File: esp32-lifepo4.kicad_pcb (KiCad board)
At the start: 2 copper layers, 15 parts, among them J1 Conn_01x12, J2 Conn_01x12, U1 ESP32-WROOM-32, U2 CN3058C, U3 TPS709

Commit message: v0
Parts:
- removed ?: , Aesthetics:OSHW-LOGO-L
- removed D1: DIODE, Diodes_SMD:D_SMA
- C2: value 4.7-10uF -> 10uF
- D2: value LED -> DONE
- D3: value LED -> CHRG
- R1: value 100 -> 100 ohms
- R2: value 2.463k -> 2.463k ohms
- R3: value 0 -> 0ohm
- U2: value CN3058C -> CN3058E
- moved JP1 0.92 mm to (166.4, 98.3)
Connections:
- C1 pad 2: Net-(C1-Pad2) -> VIN
- R1 pad 2: Net-(C1-Pad2) -> VIN
- U2 pad 4: Net-(C1-Pad2) -> VIN
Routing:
- net BAT+: track 54.9 -> 44.9 mm, vias 3 -> 1
- net Net-(C1-Pad2): track 9.95 -> 0.00 mm
- net 3V3: track 46.2 -> 42.2 mm

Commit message: minor changes
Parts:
- R2: value 2.463k ohms -> 2.463k
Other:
- board outline added: 28.4 x 31 mm
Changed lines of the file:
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@@
     (47 F.CrtYd user)
     (48 B.Fab user)
-    (49 F.Fab user)
+    (49 F.Fab user hide)
   )
   (setup
@@
     (trace_min 0.2)
     (segment_width 0.2)
-    (edge_width 0.15)
+    (edge_width 0.2)
     (via_size 0.8)
     (via_drill 0.4)
@@
     (tags "capacitor 0805")
     (attr smd)
-    (fp_text reference C1 (at -0.254 1.27 90) (layer F.SilkS)
+    (fp_text reference C1 (at -0.762 -1.524 90) (layer F.SilkS)
       (effects (font (size 1 1) (thickness 0.15)))
     )
@@
     (tags "capacitor 0805")
     (attr smd)
-    (fp_text reference C2 (at 0.762 1.778 270) (layer F.SilkS)
+    (fp_text reference C2 (at 0 1.524 270) (layer F.SilkS)
       (effects (font (size 1 1) (thickness 0.15)))
     )
@@
       (effects (font (size 0.6096 0.6096) (thickness 0.127)))
     )
-    (fp_text value "2.463k ohms" (at 0 1.27 90) (layer F.SilkS)
+    (fp_text value 2.463k (at 0 -1.27 90) (layer F.SilkS)
       (effects (font (size 0.6096 0.6096) (thickness 0.127)))
     )
@@
       (effects (font (size 0.6096 0.6096) (thickness 0.127)))
     )
-    (fp_text value 0ohm (at 0.254 -1.27 90) (layer F.SilkS)
+    (fp_text value 0ohm (at 1.016 -1.27 90) (layer F.SilkS)
       (effects (font (size 0.6096 0.6096) (thickness 0.127)))
     )
@@
     (effects (font (size 1.5 1.5) (thickness 0.3)) (justify mirror))
   )
-  (gr_line (start 143.256 100.584) (end 143.256 69.596) (layer Eco2.User) (width 0.2))
-  (gr_line (start 171.704 100.584) (end 143.256 100.584) (layer Eco2.User) (width 0.2))
-  (gr_line (start 171.704 69.596) (end 171.704 100.584) (layer Eco2.User) (width 0.2))
-  (gr_line (start 143.256 69.596) (end 171.704 69.596) (layer Eco2.User) (width 0.2))
+  (gr_line (start 143.256 100.584) (end 143.256 69.596) (layer Edge.Cuts) (width 0.2))
+  (gr_line (start 171.704 100.584) (end 143.256 100.584) (layer Edge.Cuts) (width 0.2))
+  (gr_line (start 171.704 69.596) (end 171.704 100.584) (layer Edge.Cuts) (width 0.2))
+  (gr_line (start 143.256 69.596) (end 171.704 69.596) (layer Edge.Cuts) (width 0.2))
   (via (at 153.162 96.9645) (size 0.8) (drill 0.4) (layers F.Cu B.Cu) (net 1))
   (segment (start 151.892 97.774) (end 152.3525 97.774) (width 0.25) (layer F.Cu) (net 1) (status 30))
@@
   (segment (start 157.093185 82.146599) (end 157.18 82.059784) (width 0.25) (layer F.Cu) (net 1))
   (segment (start 156.5275 82.146599) (end 157.093185 82.146599) (width 0.25) (layer F.Cu) (net 1))
-  (segment (start 154.78 96.2965) (end 154.78 96.139) (width 0.25) (layer F.Cu) (net 3) (status 30))
-  (segment (start 156.58084 98.09734) (end 154.78 96.2965) (width 0.25) (layer F.Cu) (net 3) (status 30))
-  (segment (start 156.58084 98.298) (end 156.58084 98.09734) (width 0.25) (layer F.Cu) (net 3) (status 30))
-  (segment (start 152.257 96.139) (end 151.892 95.774) (width 0.25) (layer F.Cu) (net 3) (status 30))
-  (segment (start 154.78 96.139) (end 152.257 96.139) (width 0.25) (layer F.Cu) (net 3) (status 30))
-  (segment (start 151.892 95.774) (end 151.767 95.774) (width 0.25) (layer F.Cu) (net 3) (status 30))
   (segment (start 162.703 96.139) (end 163.068 95.774) (width 0.4) (layer F.Cu) (net 2) (status 30))
   (segment (start 160.18 96.139) (end 162.703 96.139) (width 0.4) (layer F.Cu) (net 2) (status 30))
@@
   (segment (start 165.166 92.964) (end 165.1 93.03) (width 0.4) (layer F.Cu) (net 2))
   (segment (start 168.402 92.964) (end 165.166 92.964) (width 0.4) (layer F.Cu) (net 2))
+  (segment (start 154.78 96.2965) (end 154.78 96.139) (width 0.25) (layer F.Cu) (net 3) (status 30))
+  (segment (start 156.58084 98.09734) (end 154.78 96.2965) (width 0.25) (layer F.Cu) (net 3) (status 30))
+  (segment (start 156.58084 98.298) (end 156.58084 98.09734) (width 0.25) (layer F.Cu) (net 3) (status 30))
+  (segment (start 152.257 96.139) (end 151.892 95.774) (width 0.25) (layer F.Cu) (net 3) (status 30))
+  (segment (start 154.78 96.139) (end 152.257 96.139) (width 0.25) (layer F.Cu) (net 3) (status 30))
+  (segment (start 151.892 95.774) (end 151.767 95.774) (width 0.25) (layer F.Cu) (net 3) (status 30))
   (via (at 153.0985 75.8825) (size 0.8) (drill 0.4) (layers F.Cu B.Cu) (net 3))
   (segment (start 144.78 73.66) (end 150.876 73.66) (width 0.4) (layer B.Cu) (net 3) (status 10))

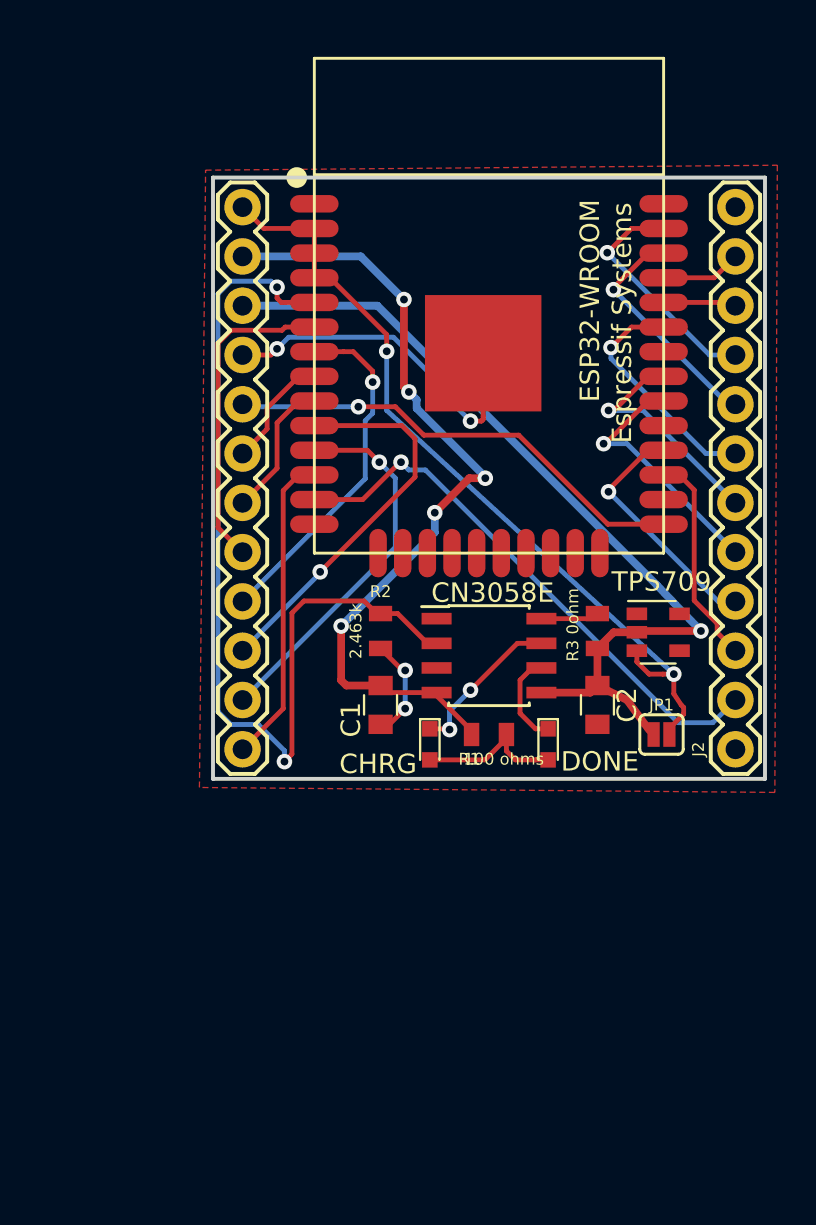
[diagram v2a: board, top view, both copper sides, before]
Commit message: Added symbol and footprint. Removed non-slim version
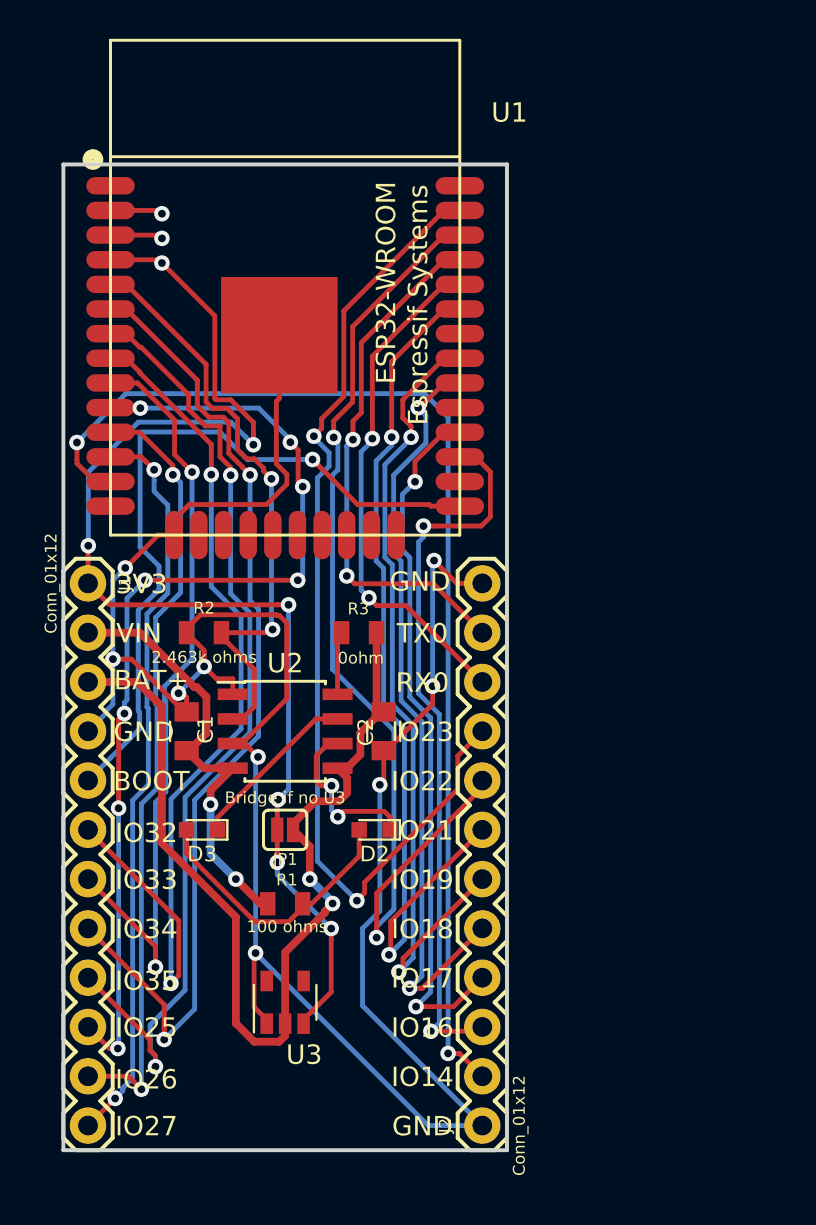
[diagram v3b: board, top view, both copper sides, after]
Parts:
- added REF***: OSHW-Symbol_13.4x12mm_SilkScreen, Symbols:OSHW-Symbol_13.4x12mm_SilkScreen, B.Cu at (147.4, 110.8)
- JP1: value SolderJumper_2_Open -> Bridge if no U3
- R2: value 2.463k -> 2.463k ohms
- moved U3 27.1 mm to (147.0, 112.1), turned to 90 degrees
- moved J2 23.4 mm to (157.1, 118.5)
- moved J1 21.0 mm to (136.8, 90.5)
- moved JP1 20.0 mm to (147.0, 103.2), turned to 180 degrees
- moved R1 13.7 mm to (147.0, 107.0)
- moved D3 12.5 mm to (142.7, 103.2), turned to 180 degrees
- moved R3 12.3 mm to (150.8, 93.1), turned to 180 degrees
- moved U2 11.2 mm to (147.0, 98.1)
- moved C2 11.1 mm to (152.1, 98.1)
- moved U1 10.5 mm to (147.0, 75.3)
- moved C1 10.1 mm to (141.9, 98.1), turned to 270 degrees
- moved D2 9.97 mm to (151.6, 103.2), turned to 180 degrees
- moved R2 9.10 mm to (142.8, 93.1), turned to 0 degrees
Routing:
- net GND: track 23.5 -> 121.5 mm, vias 4 -> 10
- net IO32: track 5.98 -> 47.8 mm, vias 0 -> 2
- net IO22: track 12.2 -> 52.2 mm, vias 1 -> 2
- net IO23: track 12.2 -> 52.0 mm, vias 1 -> 2
- net IO34: track 16.6 -> 51.1 mm, vias 0 -> 2
- net IO21: track 12.2 -> 44.9 mm, vias 1 -> 2
- net IO33: track 7.25 -> 39.5 mm, vias 0 -> 2
- net IO25: track 20.1 -> 52.1 mm, vias 1 -> 8
- net IO35: track 18.1 -> 50.0 mm, vias 1 -> 2
- net IO14: track 29.2 -> 58.9 mm, vias 1 -> 2
- net IO19: track 12.1 -> 41.5 mm, vias 1 -> 2
- net 3V3: track 42.2 -> 70.1 mm, vias 2 -> 9
- net IO16: track 11.1 -> 37.4 mm, vias 0 -> 2
- net IO18: track 13.1 -> 39.3 mm, vias 1 -> 2
- net IO17: track 12.7 -> 36.2 mm, vias 1 -> 2
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- added copper zone on B.Cu, net 3V3
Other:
- board size 28.4 x 31 mm -> 22.9 x 50.8 mm
- board text added: "IO14"
- board text added: "IO16"
- board text added: "IO17"
- board text added: "IO18"
- board text added: "IO19"
- board text added: "IO21"
- board text added: "IO22"
- board text added: "IO23"
- board text added: "IO25"
- board text added: "IO26"
- board text added: "IO27"
- board text added: "IO32"
- board text added: "IO33"
- board text added: "IO34"
- board text added: "IO35"
- board text added: "RX0"
- board text added: "TX0"
- board text added: "VIN"
- board text added: "[ ESP32 / LiFePo4 ]"
- board text added: "github.com/pho/esp32-lifepo4-board"
- board text removed: "14"
- board text removed: "16"
- board text removed: "17"
- board text removed: "18"
- board text removed: "19"
- board text removed: "21"
- board text removed: "22"
- board text removed: "23"
- board text removed: "25"
- board text removed: "26"
- board text removed: "27"
- board text removed: "32"
- board text removed: "33"
- board text removed: "34"
- board text removed: "35"
- board text removed: "5V VIN"
- board text removed: "RX"
- board text removed: "TX"
